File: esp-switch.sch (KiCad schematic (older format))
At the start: 23 parts, among them J1 Screw_Terminal_01x03, J2 Conn_01x04, J4 Conn_01x04, J5 Screw_Terminal_01x02, U1 ATTINY441-SSU, U2 ESP-01v090, U3 MOC3041M, U4 MOC3041M, U5 HLK-PM05

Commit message: Polishing
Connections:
- net at J2.1 (Pin_1), U1.9 ((PCINT4/SCK/SCL/RXD1/T1/TOCC3/AIN11/ADC4)PA4): now also U2.4 (GPIO2)
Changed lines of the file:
@@
 	1    0    0    -1
 $EndComp
-Wire Wire Line
-	4150 2700 3950 2700
-Wire Wire Line
-	3950 2700 3950 1300
-Wire Wire Line
-	3950 1300 3600 1300
-Wire Wire Line
-	6200 3000 6050 3000
-Wire Wire Line
-	1200 2300 1500 2300
 $Comp
 L +5V #PWR01
@@
 	1    0    0    -1
 $EndComp
-Wire Wire Line
-	1200 1100 1200 750
 $Comp
 L GND #PWR03
@@
 	1    0    0    -1
 $EndComp
-Wire Wire Line
-	6050 2700 6500 2700
-Wire Wire Line
-	6500 2700 6500 2800
 $Comp
 L +5V #PWR04
@@
 	1    0    0    -1
 $EndComp
-Wire Wire Line
-	4150 3000 4050 3000
 $Comp
 L GND #PWR05
@@
 	1    0    0    -1
 $EndComp
-Wire Wire Line
-	7950 3600 7950 3750
-Wire Wire Line
-	7350 3750 8300 3750
-Wire Wire Line
-	8300 3750 8300 3600
-Wire Wire Line
-	8100 3750 8100 3850
-Connection ~ 8100 3750
-Wire Wire Line
-	7950 3000 7950 3300
-Wire Wire Line
-	8300 3300 8300 3100
-Wire Wire Line
-	8350 2550 8350 2900
-Wire Wire Line
-	7150 2550 8350 2550
 $Comp
 L TRIAC_TTG D3
@@
 	0    1    1    0
 $EndComp
-Wire Wire Line
-	8950 2900 9000 2900
-Wire Wire Line
-	9000 2900 9000 2550
-Wire Wire Line
-	9000 2550 9100 2550
 $Comp
 L R R6
@@
 	0    1    1    0
 $EndComp
-Wire Wire Line
-	9000 3100 9000 3400
-Wire Wire Line
-	9000 3400 9100 3400
-Connection ~ 9000 3100
-Wire Wire Line
-	8300 3100 8350 3100
-Wire Wire Line
-	7950 2700 7950 2550
-Connection ~ 7950 2550
-Wire Wire Line
-	9350 3100 8950 3100
-Wire Wire Line
-	9500 3150 9500 3400
-Connection ~ 9500 3400
-Wire Wire Line
-	9500 2550 9500 2850
-Connection ~ 9500 2550
 $Comp
 L MOC3041M U4
@@
 	1    0    0    -1
 $EndComp
-Wire Wire Line
-	7950 5450 7950 5600
-Wire Wire Line
-	7950 5600 8300 5600
-Wire Wire Line
-	8300 5600 8300 5450
-Wire Wire Line
-	8100 5600 8100 5700
-Connection ~ 8100 5600
-Wire Wire Line
-	7950 4850 7950 5150
-Wire Wire Line
-	8300 5150 8300 4950
-Wire Wire Line
-	8350 4400 8350 4750
-Wire Wire Line
-	6700 4400 8350 4400
 $Comp
 L TRIAC_TTG D4
@@
 	0    1    1    0
 $EndComp
-Wire Wire Line
-	8950 4750 9000 4750
-Wire Wire Line
-	9000 4750 9000 4400
-Wire Wire Line
-	9000 4400 9100 4400
 $Comp
 L R R8
@@
 	0    1    1    0
 $EndComp
-Wire Wire Line
-	9000 4950 9000 5250
-Wire Wire Line
-	9000 5250 9100 5250
-Connection ~ 9000 4950
-Wire Wire Line
-	8300 4950 8350 4950
-Wire Wire Line
-	7950 4550 7950 4400
-Connection ~ 7950 4400
-Wire Wire Line
-	9350 4950 8950 4950
-Wire Wire Line
-	9500 5000 9500 5250
-Connection ~ 9500 5250
-Wire Wire Line
-	9500 4400 9500 4700
-Connection ~ 9500 4400
-Wire Wire Line
-	9900 5250 9400 5250
-Wire Wire Line
-	9650 2550 9400 2550
-Wire Wire Line
-	9650 4400 9400 4400
 $Comp
 L Conn_01x04 J4
@@
 	-1   0    0    -1
 $EndComp
-Wire Wire Line
-	7150 3300 7050 3300
-Wire Wire Line
-	7150 2000 7150 3300
-Wire Wire Line
-	7050 3400 7150 3400
-Wire Wire Line
-	7150 3400 7150 4400
-Wire Wire Line
-	7050 3600 7350 3600
-Wire Wire Line
-	7350 3600 7350 3750
-Connection ~ 7950 3750
 $Comp
 L +5V #PWR09
@@
 	1    0    0    -1
 $EndComp
-Wire Wire Line
-	7050 3500 7400 3500
-Wire Wire Line
-	7400 3500 7400 3350
 $Comp
 L HLK-PM05 U5
@@
 	1    0    0    -1
 $EndComp
-Wire Wire Line
-	9900 1500 9750 1500
-Wire Wire Line
-	9900 1600 9750 1600
 $Comp
 L GND #PWR010
@@
 	1    0    0    -1
 $EndComp
-Wire Wire Line
-	9150 1600 9050 1600
-Wire Wire Line
-	9050 1600 9050 1700
-Wire Wire Line
-	9150 1500 9050 1500
-Wire Wire Line
-	9050 1500 9050 1450
-Wire Wire Line
-	1200 2300 1200 2500
-Wire Wire Line
-	1200 1100 1500 1100
 $Comp
 L Screw_Terminal_01x03 J1
@@
 	1    0    0    1
 $EndComp
-Wire Wire Line
-	9900 3400 9400 3400
 $Comp
 L Fuse_Small F1
@@
 	1    0    0    -1
 $EndComp
-Wire Wire Line
-	9650 2550 9650 4400
-Wire Wire Line
-	10050 3550 9650 3550
-Connection ~ 9650 3550
-Wire Wire Line
-	10250 3550 10450 3550
-Wire Wire Line
-	9900 3400 9900 3650
-Wire Wire Line
-	9900 3650 10450 3650
-Wire Wire Line
-	9900 5250 9900 3750
-Wire Wire Line
-	9900 3750 10450 3750
 $Comp
 L RF_Receiver_EV1527 RF1
@@
 	1    0    0    -1
 $EndComp
-Wire Wire Line
-	6200 3000 6200 3300
-Wire Wire Line
-	6200 3300 3850 3300
-Wire Wire Line
-	3850 3300 3850 1200
-Wire Wire Line
-	3850 1200 3600 1200
-Wire Wire Line
-	7450 1350 7450 1400
-Wire Wire Line
-	7450 1400 7100 1400
-Wire Wire Line
-	7100 1400 7100 900
-Wire Wire Line
-	7550 1350 7550 1450
-Wire Wire Line
-	5100 1450 7850 1450
-Wire Wire Line
-	7850 1450 7850 1350
-Wire Wire Line
-	7750 1550 7750 1350
-Wire Wire Line
-	5000 1550 7750 1550
-Wire Wire Line
-	7650 1550 7650 1350
 $Comp
 L Conn_01x04 J2
@@
 	1    0    0    -1
 $EndComp
-Wire Wire Line
-	3600 1500 4100 1500
+NoConn ~ 8150 1350
+Wire Wire Line
+	4150 2700 3950 2700
+Wire Wire Line
+	3950 2700 3950 1300
+Wire Wire Line
+	3950 1300 3600 1300
+Wire Wire Line
+	6200 3000 6050 3000
+Wire Wire Line
+	1200 2300 1500 2300
+Wire Wire Line
+	1200 1100 1200 750
+Wire Wire Line
+	6050 2700 6500 2700
+Wire Wire Line
+	6500 2700 6500 2800
+Wire Wire Line
+	4150 3000 4050 3000
+Wire Wire Line
+	7950 3600 7950 3750
+Wire Wire Line
+	7350 3750 8300 3750
+Wire Wire Line
+	8300 3750 8300 3600
+Wire Wire Line
+	8100 3750 8100 3850
+Connection ~ 8100 3750
+Wire Wire Line
+	7950 3000 7950 3300
+Wire Wire Line
+	8300 3300 8300 3100
+Wire Wire Line
+	8350 2550 8350 2900
+Wire Wire Line
+	7150 2550 8350 2550
+Wire Wire Line
+	8950 2900 9000 2900
+Wire Wire Line
+	9000 2900 9000 2550
+Wire Wire Line
+	9000 2550 9100 2550
+Wire Wire Line
+	9000 3100 9000 3400
+Wire Wire Line
+	9000 3400 9100 3400
+Connection ~ 9000 3100
+Wire Wire Line
+	8300 3100 8350 3100
+Wire Wire Line
+	7950 2700 7950 2550
+Connection ~ 7950 2550
+Wire Wire Line
+	9350 3100 8950 3100
+Wire Wire Line
+	9500 3150 9500 3400
+Connection ~ 9500 3400
+Wire Wire Line
+	9500 2550 9500 2850
+Connection ~ 9500 2550
+Wire Wire Line
+	7950 5450 7950 5600
+Wire Wire Line
+	7950 5600 8300 5600
+Wire Wire Line
+	8300 5600 8300 5450
+Wire Wire Line
+	8100 5600 8100 5700
+Connection ~ 8100 5600
+Wire Wire Line
+	7950 4850 7950 5150
+Wire Wire Line
+	8300 5150 8300 4950
+Wire Wire Line
+	8350 4400 8350 4750
+Wire Wire Line
+	6700 4400 8350 4400
+Wire Wire Line
+	8950 4750 9000 4750
+Wire Wire Line
+	9000 4750 9000 4400
+Wire Wire Line
+	9000 4400 9100 4400
+Wire Wire Line
+	9000 4950 9000 5250
+Wire Wire Line
+	9000 5250 9100 5250
+Connection ~ 9000 4950
+Wire Wire Line
+	8300 4950 8350 4950
+Wire Wire Line
+	7950 4550 7950 4400
+Connection ~ 7950 4400
+Wire Wire Line
+	9350 4950 8950 4950
+Wire Wire Line
+	9500 5000 9500 5250
+Connection ~ 9500 5250
+Wire Wire Line
+	9500 4400 9500 4700
+Connection ~ 9500 4400
+Wire Wire Line
+	9900 5250 9400 5250
+Wire Wire Line
+	9650 2550 9400 2550
+Wire Wire Line
+	9650 4400 9400 4400
+Wire Wire Line
+	7150 3300 7050 3300
+Wire Wire Line
+	7150 2000 7150 3300
+Wire Wire Line
+	7050 3400 7150 3400
+Wire Wire Line
+	7150 3400 7150 4400
+Wire Wire Line
+	7050 3600 7350 3600
+Wire Wire Line
+	7350 3600 7350 3750
+Connection ~ 7950 3750
+Wire Wire Line
+	7050 3500 7400 3500
+Wire Wire Line
+	7400 3500 7400 3350
+Wire Wire Line
+	9900 1500 9750 1500
+Wire Wire Line
+	9900 1600 9750 1600
+Wire Wire Line
+	9150 1600 9050 1600
+Wire Wire Line
+	9050 1600 9050 1700
+Wire Wire Line
+	9150 1500 9050 1500
+Wire Wire Line
+	9050 1500 9050 1450
+Wire Wire Line
+	1200 2300 1200 2500
+Wire Wire Line
+	1200 1100 1500 1100
+Wire Wire Line
+	9900 3400 9400 3400
+Wire Wire Line
+	9650 2550 9650 4400
+Wire Wire Line
+	10050 3550 9650 3550
+Connection ~ 9650 3550
+Wire Wire Line
+	10250 3550 10450 3550
+Wire Wire Line
+	9900 3400 9900 3650
+Wire Wire Line
+	9900 3650 10450 3650
+Wire Wire Line
+	9900 5250 9900 3750
+Wire Wire Line
+	9900 3750 10450 3750
+Wire Wire Line
+	6200 3000 6200 3300
+Wire Wire Line
+	6200 3300 3850 3300
+Wire Wire Line
+	3850 3300 3850 1200
+Wire Wire Line
+	3850 1200 3600 1200
+Wire Wire Line
+	7450 1350 7450 1400
+Wire Wire Line
+	7450 1400 7100 1400
+Wire Wire Line
+	7100 1400 7100 900
+Wire Wire Line
+	7550 1350 7550 1450
+Wire Wire Line
+	5100 1450 7850 1450
+Wire Wire Line
+	7850 1450 7850 1350
+Wire Wire Line
+	7750 1550 7750 1350
+Wire Wire Line
+	5000 1550 7750 1550
+Wire Wire Line
+	7650 1550 7650 1350
+Wire Wire Line
+	3600 1500 4700 1500
 Wire Wire Line
 	4100 1500 4100 650
@@
 Wire Wire Line
 	8050 2200 8050 1350
-NoConn ~ 8150 1350
 Wire Wire Line
 	4150 2800 4050 2800
@@
 	4150 2900 4050 2900
 Connection ~ 4050 2900
+Wire Wire Line
+	4700 1500 4700 1700
+Wire Wire Line
+	4700 1700 6200 1700
+Wire Wire Line
+	6200 1700 6200 2800
+Wire Wire Line
+	6200 2800 6050 2800
+Connection ~ 4100 1500
 $EndSCHEMATC

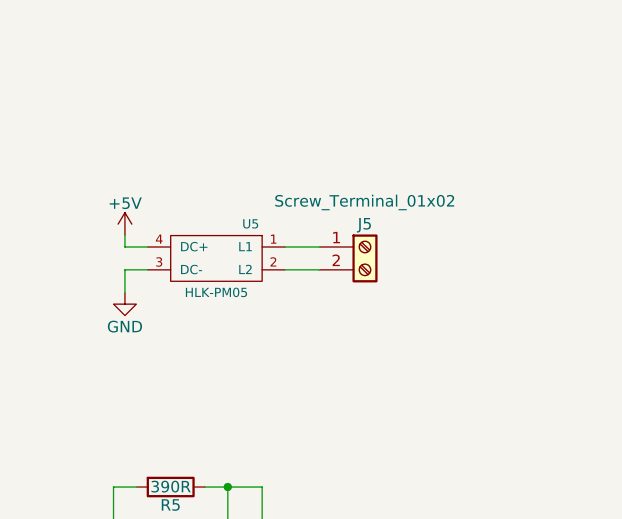
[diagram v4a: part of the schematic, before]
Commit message: Power circuit fuse
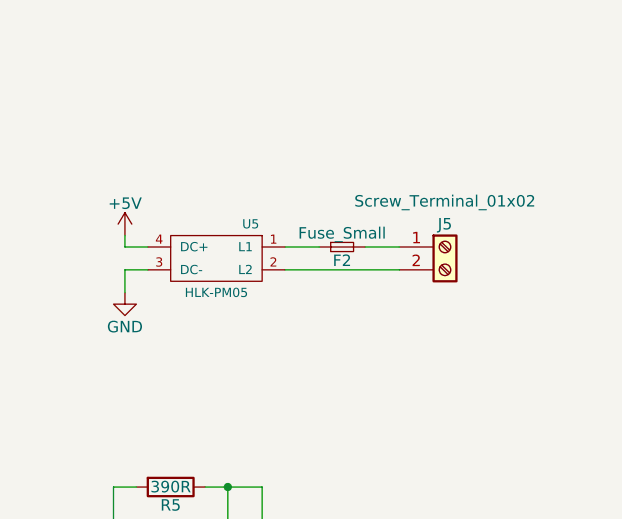
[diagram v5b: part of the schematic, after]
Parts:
- added F2: Fuse_Small, Resistors_THT:R_Axial_DIN0207_L6.3mm_D2.5mm_P7.62mm_Horizontal, symbol Fuse_Small
- F1: footprint Resistors_THT:R_Axial_DIN0411_L9.9mm_D3.6mm_P12.70mm_Horizontal -> Resistors_THT:R_Axial_DIN0207_L6.3mm_D2.5mm_P7.62mm_Horizontal
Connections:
- net at U5.1 (L1): now also F2.1; no longer J5.1 (Pin_1)
- new net: F2.2, J5.1 (Pin_1)
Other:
- moved on the sheet: J5
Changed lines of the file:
@@
 L Screw_Terminal_01x02 J5
 U 1 1 5A558F98
-P 10100 1500
-F 0 "J5" H 10100 1600 50  0000 C CNN
-F 1 "Screw_Terminal_01x02" H 10100 1700 50  0000 C CNN
-F 2 "Connectors_Terminal_Blocks:TerminalBlock_Pheonix_MKDS1.5-2pol" H 10100 1500 50  0001 C CNN
-F 3 "" H 10100 1500 50  0001 C CNN
-	1    10100 1500
+P 10450 1500
+F 0 "J5" H 10450 1600 50  0000 C CNN
+F 1 "Screw_Terminal_01x02" H 10450 1700 50  0000 C CNN
+F 2 "Connectors_Terminal_Blocks:TerminalBlock_Pheonix_MKDS1.5-2pol" H 10450 1500 50  0001 C CNN
+F 3 "" H 10450 1500 50  0001 C CNN
+	1    10450 1500
 	1    0    0    -1
 $EndComp
@@
 F 0 "F1" H 10150 3490 50  0000 C CNN
 F 1 "Fuse_Small" H 10150 3610 50  0000 C CNN
-F 2 "Resistors_THT:R_Axial_DIN0411_L9.9mm_D3.6mm_P12.70mm_Horizontal" H 10150 3550 50  0001 C CNN
+F 2 "Resistors_THT:R_Axial_DIN0207_L6.3mm_D2.5mm_P7.62mm_Horizontal" H 10150 3550 50  0001 C CNN
 F 3 "" H 10150 3550 50  0001 C CNN
 	1    10150 3550
@@
 	9900 1500 9750 1500
 Wire Wire Line
-	9900 1600 9750 1600
+	9750 1600 10250 1600
 Wire Wire Line
 	9150 1600 9050 1600
@@
 	6200 2800 6050 2800
 Connection ~ 4100 1500
+$Comp
+L Fuse_Small F2
+U 1 1 5A6693E1
+P 10000 1500
+F 0 "F2" H 10000 1440 50  0000 C CNN
+F 1 "Fuse_Small" H 10000 1560 50  0000 C CNN
+F 2 "Resistors_THT:R_Axial_DIN0207_L6.3mm_D2.5mm_P7.62mm_Horizontal" H 10000 1500 50  0001 C CNN
+F 3 "" H 10000 1500 50  0001 C CNN
+	1    10000 1500
+	1    0    0    -1
+$EndComp
+Wire Wire Line
+	10100 1500 10250 1500
 $EndSCHEMATC

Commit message: Capasitor
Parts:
- added C1: CP_Small, Capacitors_THT:CP_Radial_D4.0mm_P2.00mm, symbol CP_Small
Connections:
- net +5V: now also C1.1
- net GND: now also C1.2
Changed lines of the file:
@@
 Wire Wire Line
 	10100 1500 10250 1500
+$Comp
+L CP_Small C1
+U 1 1 5A669960
+P 8750 1550
+F 0 "C1" H 8760 1620 50  0000 L CNN
+F 1 "CP_Small" H 8760 1470 50  0000 L CNN
+F 2 "Capacitors_THT:CP_Radial_D4.0mm_P2.00mm" H 8750 1550 50  0001 C CNN
+F 3 "" H 8750 1550 50  0001 C CNN
+	1    8750 1550
+	1    0    0    -1
+$EndComp
+$Comp
+L +5V #PWR012
+U 1 1 5A669A9B
+P 8750 1350
+F 0 "#PWR012" H 8750 1200 50  0001 C CNN
+F 1 "+5V" H 8750 1490 50  0000 C CNN
+F 2 "" H 8750 1350 50  0001 C CNN
+F 3 "" H 8750 1350 50  0001 C CNN
+	1    8750 1350
+	1    0    0    -1
+$EndComp
+$Comp
+L GND #PWR013
+U 1 1 5A669AF1
+P 8750 1700
+F 0 "#PWR013" H 8750 1450 50  0001 C CNN
+F 1 "GND" H 8750 1550 50  0000 C CNN
+F 2 "" H 8750 1700 50  0001 C CNN
+F 3 "" H 8750 1700 50  0001 C CNN
+	1    8750 1700
+	1    0    0    -1
+$EndComp
+Wire Wire Line
+	8750 1650 8750 1700
+Wire Wire Line
+	8750 1350 8750 1450
 $EndSCHEMATC

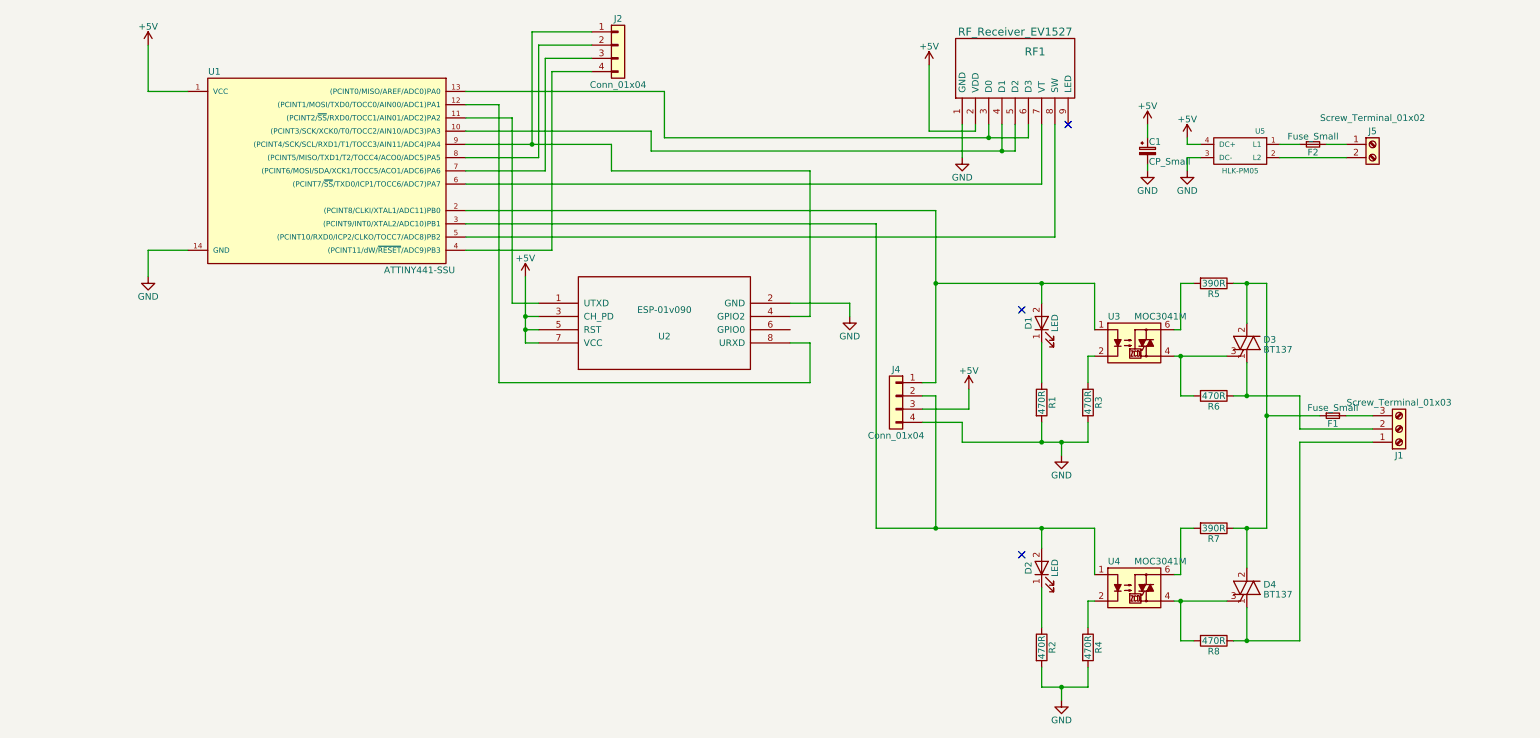
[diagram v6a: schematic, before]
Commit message: V2 - traced all the channels from RF
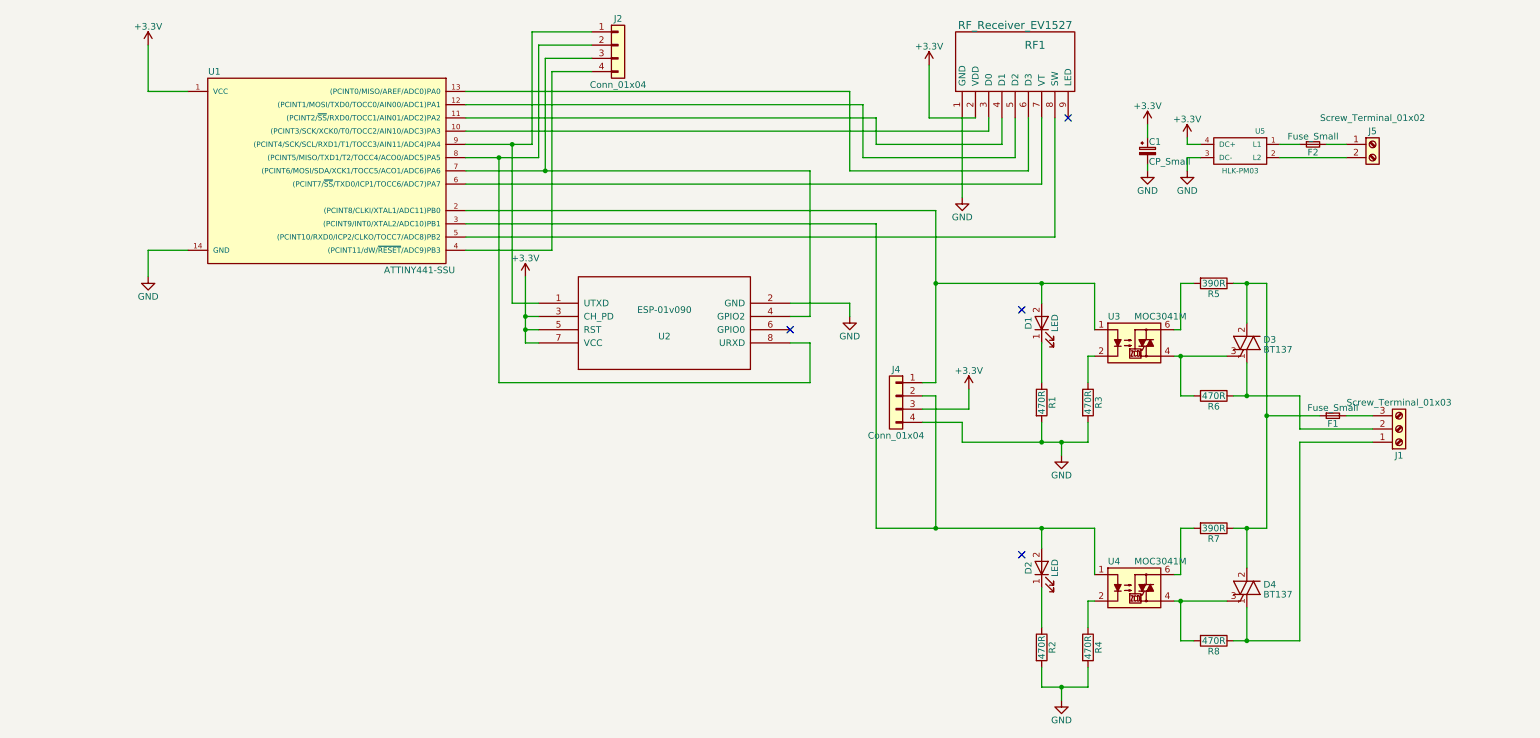
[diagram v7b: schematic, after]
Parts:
- U5: value HLK-PM05 -> HLK-PM03
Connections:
- net at U1.11 ((PCINT2/~SS~/RXD0/TOCC1/AIN01/ADC2)PA2): now also RF1.4 (D1); no longer U2.1 (UTXD)
- net at U1.12 ((PCINT1/MOSI/TXD0/TOCC0/AIN00/ADC1)PA1): now also RF1.5 (D2); no longer U2.8 (URXD)
- net at RF1.6 (D3), U1.13 ((PCINT0/MISO/AREF/ADC0)PA0): no longer RF1.3 (D0)
- net at J2.3 (Pin_3), U1.7 ((PCINT6/MOSI/SDA/XCK1/TOCC5/ACO1/ADC6)PA6): now also U2.4 (GPIO2)
- net at J2.2 (Pin_2), U1.8 ((PCINT5/MISO/TXD1/T2/TOCC4/ACO0/ADC5)PA5): now also U2.8 (URXD)
- net at J2.1 (Pin_1), U1.9 ((PCINT4/SCK/SCL/RXD1/T1/TOCC3/AIN11/ADC4)PA4): now also U2.1 (UTXD); no longer U2.4 (GPIO2)
- net +5V renamed +3V3
- new net: RF1.3 (D0), U1.10 ((PCINT3/SCK/XCK0/T0/TOCC2/AIN10/ADC3)PA3)
- no-connect marks 3 -> 4
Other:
- moved on the sheet: RF1

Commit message: Changed components
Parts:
- D3, D4: value BT137 -> BTA08-600BW
- R3, R4: value 470R -> 150R
- U3, U4: value MOC3041M -> MOC3043M
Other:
- note added: "We want to make source current from TINY to be <= 10 mA.\nSo we use MOC3043/MOC3063 - see last '3' here \nstands for modification with trigger current of 5 mA.\nThe Red LED is set up to drain less than 2 mA."
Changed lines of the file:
@@
 P 8650 3000
 F 0 "U3" H 8450 3200 50  0000 L CNN
-F 1 "MOC3041M" H 8650 3200 50  0000 L CNN
+F 1 "MOC3043M" H 8650 3200 50  0000 L CNN
 F 2 "Housings_DIP:DIP-6_W7.62mm" H 8450 2800 50  0001 L CIN
 F 3 "" H 8615 3000 50  0001 L CNN
@@
 P 8300 3450
 F 0 "R3" V 8380 3450 50  0000 C CNN
-F 1 "470R" V 8300 3450 50  0000 C CNN
+F 1 "150R" V 8300 3450 50  0000 C CNN
 F 2 "Resistors_THT:R_Axial_DIN0207_L6.3mm_D2.5mm_P2.54mm_Vertical" V 8230 3450 50  0001 C CNN
 F 3 "" H 8300 3450 50  0001 C CNN
@@
 P 9500 3000
 F 0 "D3" H 9625 3025 50  0000 L CNN
-F 1 "BT137" H 9625 2950 50  0000 L CNN
+F 1 "BTA08-600BW" H 9625 2950 50  0000 L CNN
 F 2 "TO_SOT_Packages_THT:TO-220_Vertical" V 9575 3025 50  0001 C CNN
 F 3 "" V 9500 3000 50  0001 C CNN
@@
 P 8650 4850
 F 0 "U4" H 8450 5050 50  0000 L CNN
-F 1 "MOC3041M" H 8650 5050 50  0000 L CNN
+F 1 "MOC3043M" H 8650 5050 50  0000 L CNN
 F 2 "Housings_DIP:DIP-6_W7.62mm" H 8450 4650 50  0001 L CIN
 F 3 "" H 8615 4850 50  0001 L CNN
@@
 P 8300 5300
 F 0 "R4" V 8380 5300 50  0000 C CNN
-F 1 "470R" V 8300 5300 50  0000 C CNN
+F 1 "150R" V 8300 5300 50  0000 C CNN
 F 2 "Resistors_THT:R_Axial_DIN0207_L6.3mm_D2.5mm_P2.54mm_Vertical" V 8230 5300 50  0001 C CNN
 F 3 "" H 8300 5300 50  0001 C CNN
@@
 P 9500 4850
 F 0 "D4" H 9625 4875 50  0000 L CNN
-F 1 "BT137" H 9625 4800 50  0000 L CNN
+F 1 "BTA08-600BW" H 9625 4800 50  0000 L CNN
 F 2 "TO_SOT_Packages_THT:TO-220_Vertical" V 9575 4875 50  0001 C CNN
 F 3 "" V 9500 4850 50  0001 C CNN
@@
 	1    0    0    -1
 $EndComp
+Text Notes 8300 2400 0    60   ~ 0
+We want to make source current from TINY to be <= 10 mA.\nSo we use MOC3043/MOC3063 - see last '3' here \nstands for modification with trigger current of 5 mA.\nThe Red LED is set up to drain less than 2 mA.
 $EndSCHEMATC
